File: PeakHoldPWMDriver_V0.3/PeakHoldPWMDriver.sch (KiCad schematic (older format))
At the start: 113 parts, among them J1 RND 205-00203, J2 RND 205-00205, Q1 2N7002, Q10 2N7002, Q11 2N7002, Q12 2N7002, Q13 TSM2309, Q14 IRLL 024N, Q15 TSM2309, Q16 IRLL 024N, Q2 2N7002, Q3 2N7002, Q4 2N7002, Q5 TSM2309, Q6 TSM2309, Q7 IRLL 024N, Q8 IRLL 024N, Q9 2N7002, U1 74LS32, U2 LM2901, U3 74LS74, U4 LTC6992, U5 74LS74, U6 LM340, U7 74LS08, U8 74LS08

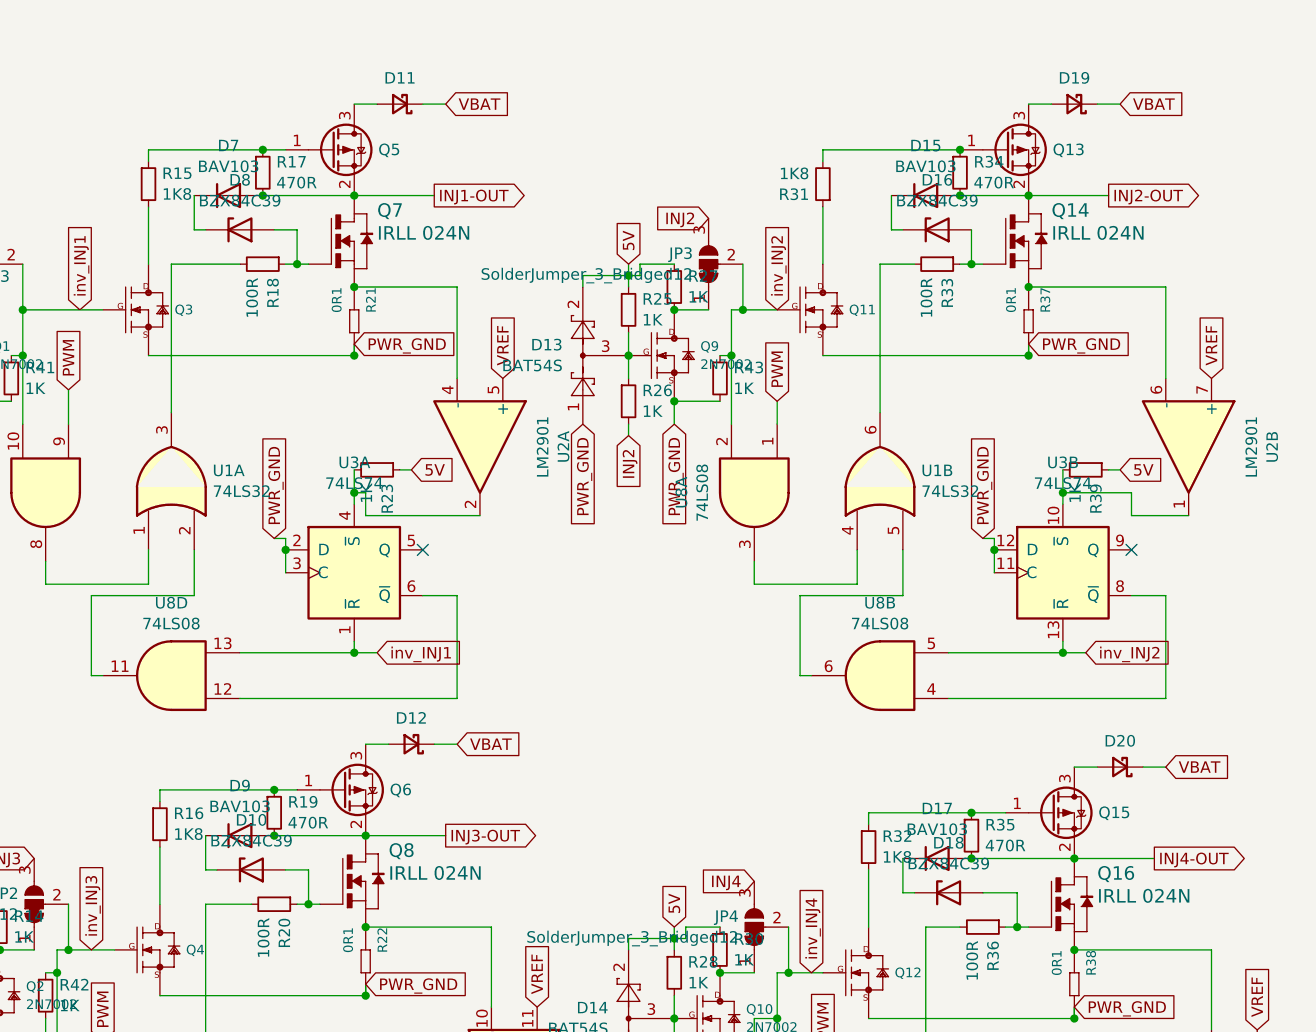
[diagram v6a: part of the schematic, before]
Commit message: update on p-chan mosfets
Overheating issues hopefully solved by this mod
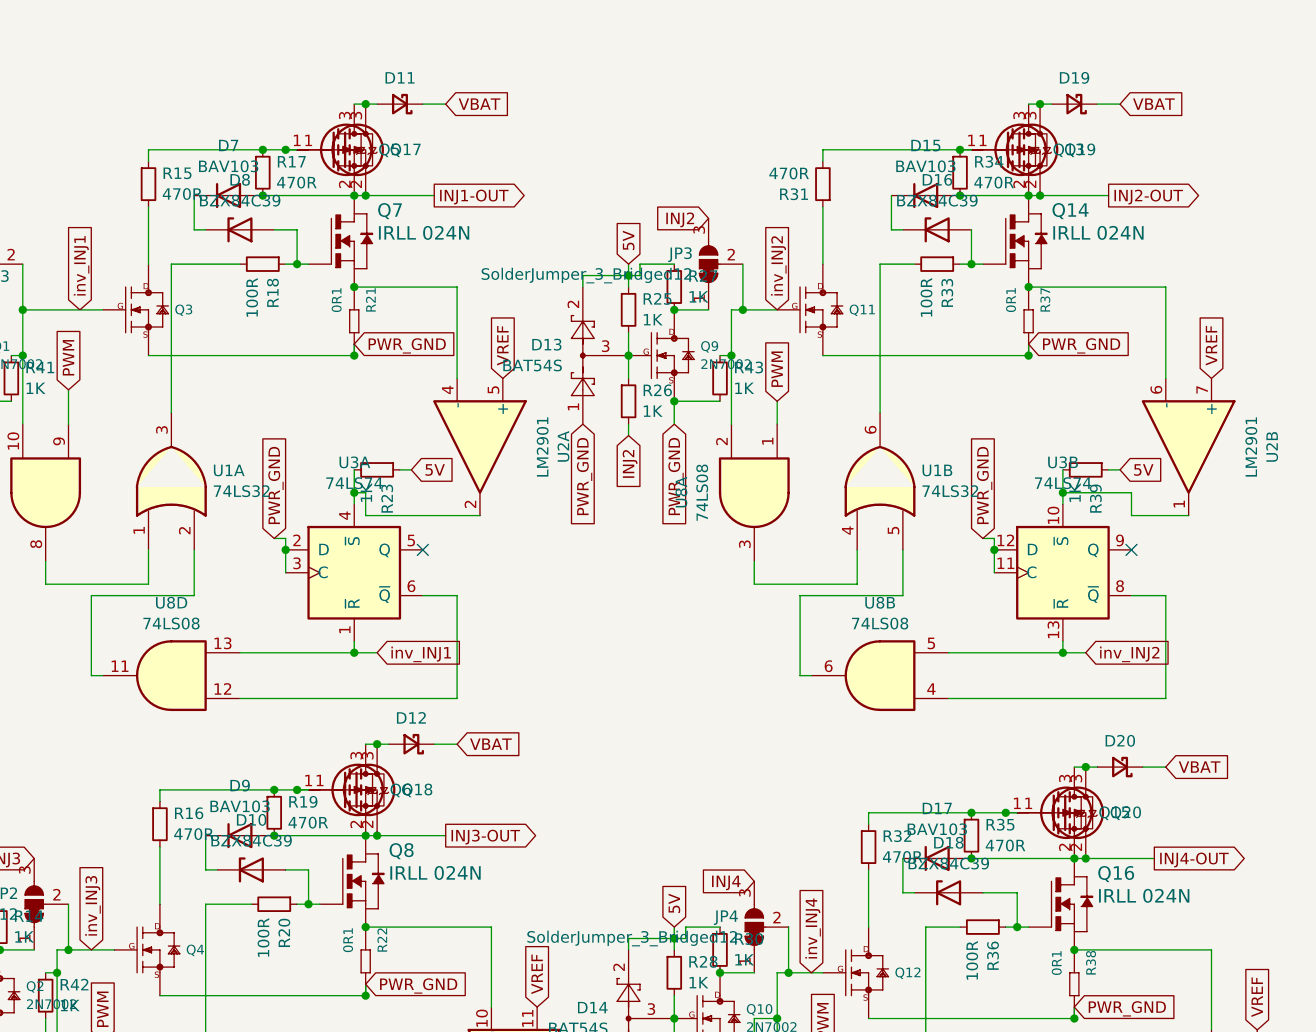
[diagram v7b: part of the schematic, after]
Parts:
- added Q17, Q18, Q19, Q20: TSM2309, Package_TO_SOT_SMD:SOT-23, symbol Transistor_FET:AO3401A
- Q13, Q15, Q5, Q6: footprint Package_TO_SOT_SMD:SOT-23_Handsoldering -> Package_TO_SOT_SMD:SOT-23
- R15, R16, R31, R32: value 1K8 -> 470R
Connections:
- net INJ1-OUT: now also Q17.2 (S)
- net INJ2-OUT: now also Q19.2 (S)
- net INJ3-OUT: now also Q18.2 (S)
- net INJ4-OUT: now also Q20.2 (S)
- net at Q13.1 (G), R31.2, R34.1: now also Q19.1 (G)
- net at D19.2 (A), Q13.3 (D): now also Q19.3 (D)
- net at Q15.1 (G), R32.1, R35.1: now also Q20.1 (G)
- net at Q5.1 (G), R15.1, R17.1: now also Q17.1 (G)
- net at D11.2 (A), Q5.3 (D): now also Q17.3 (D)
- net at Q6.1 (G), R16.1, R19.1: now also Q18.1 (G)
- net at D12.2 (A), Q6.3 (D): now also Q18.3 (D)
- net at D20.2 (A), Q15.3 (D): now also Q20.3 (D)
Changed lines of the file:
@@
 F 0 "Q5" H 7205 1100 50  0000 L CNN
 F 1 "TSM2309" H 7205 1055 50  0001 L CNN
-F 2 "Package_TO_SOT_SMD:SOT-23_Handsoldering" H 7200 1025 50  0001 L CIN
+F 2 "Package_TO_SOT_SMD:SOT-23" H 7200 1025 50  0001 L CIN
 F 3 "https://www.mouser.com/datasheet/2/395/TSM2309_A15-1116136.pdf" H 7000 1100 50  0001 L CNN
 	1    7000 1100
@@
 F 0 "Q15" H 10355 4000 50  0000 L CNN
 F 1 "TSM2309" H 10355 3955 50  0001 L CNN
-F 2 "Package_TO_SOT_SMD:SOT-23_Handsoldering" H 10350 3925 50  0001 L CIN
+F 2 "Package_TO_SOT_SMD:SOT-23" H 10350 3925 50  0001 L CIN
 F 3 "http://www.aosmd.com/pdfs/datasheet/AO3401A.pdf" H 10150 4000 50  0001 L CNN
 	1    10150 4000
@@
 P 9350 4150
 F 0 "R32" H 9409 4196 50  0000 L CNN
-F 1 "1K8" H 9409 4105 50  0000 L CNN
+F 1 "470R" H 9409 4105 50  0000 L CNN
 F 2 "Resistor_SMD:R_0603_1608Metric_Pad1.05x0.95mm_HandSolder" H 9350 4150 50  0001 C CNN
 F 3 "~" H 9350 4150 50  0001 C CNN
@@
 F 0 "Q13" H 10155 1100 50  0000 L CNN
 F 1 "TSM2309" H 10155 1055 50  0001 L CNN
-F 2 "Package_TO_SOT_SMD:SOT-23_Handsoldering" H 10150 1025 50  0001 L CIN
+F 2 "Package_TO_SOT_SMD:SOT-23" H 10150 1025 50  0001 L CIN
 F 3 "http://www.aosmd.com/pdfs/datasheet/AO3401A.pdf" H 9950 1100 50  0001 L CNN
 	1    9950 1100
@@
 F 0 "Q6" H 7255 3900 50  0000 L CNN
 F 1 "TSM2309" H 7255 3855 50  0001 L CNN
-F 2 "Package_TO_SOT_SMD:SOT-23_Handsoldering" H 7250 3825 50  0001 L CIN
+F 2 "Package_TO_SOT_SMD:SOT-23" H 7250 3825 50  0001 L CIN
 F 3 "http://www.aosmd.com/pdfs/datasheet/AO3401A.pdf" H 7050 3900 50  0001 L CNN
 	1    7050 3900
@@
 P 6250 4050
 F 0 "R16" H 6309 4096 50  0000 L CNN
-F 1 "1K8" H 6309 4005 50  0000 L CNN
+F 1 "470R" H 6309 4005 50  0000 L CNN
 F 2 "Resistor_SMD:R_0603_1608Metric_Pad1.05x0.95mm_HandSolder" H 6250 4050 50  0001 C CNN
 F 3 "~" H 6250 4050 50  0001 C CNN
@@
 P 6200 1250
 F 0 "R15" H 6259 1296 50  0000 L CNN
-F 1 "1K8" H 6259 1205 50  0000 L CNN
+F 1 "470R" H 6259 1205 50  0000 L CNN
 F 2 "Resistor_SMD:R_0603_1608Metric_Pad1.05x0.95mm_HandSolder" H 6200 1250 50  0001 C CNN
 F 3 "~" H 6200 1250 50  0001 C CNN
@@
 Connection ~ 7150 4100
 Wire Wire Line
-	7150 3700 7250 3700
+	7150 3700 7200 3700
 Wire Wire Line
 	6250 4400 6250 4150
@@
 PWR_GND
 Wire Wire Line
-	10050 1300 10400 1300
+	10050 1300 10100 1300
 Wire Wire Line
 	10450 900  10350 900
 Connection ~ 10050 1300
 Wire Wire Line
-	10050 900  10150 900
+	10050 900  10100 900
 Wire Wire Line
 	9150 1600 9150 1350
@@
 Connection ~ 10250 4200
 Wire Wire Line
-	10250 3800 10350 3800
+	10250 3800 10300 3800
 Wire Wire Line
 	9350 4500 9350 4250
@@
 Connection ~ 7100 1300
 Wire Wire Line
-	7100 1300 7450 1300
-Wire Wire Line
-	7100 900  7200 900
+	7100 1300 7150 1300
+Wire Wire Line
+	7100 900  7150 900
 Wire Wire Line
 	6700 1300 7100 1300
@@
 	10250 4200 9800 4200
 Wire Wire Line
-	7150 4100 7500 4100
+	7150 4100 7200 4100
 $Comp
 L Comparator:LM2901 U2
@@
 Connection ~ 6750 3900
 Wire Wire Line
-	6750 3900 6850 3900
-Wire Wire Line
 	9350 4000 9800 4000
 Connection ~ 9800 4000
 Wire Wire Line
-	9800 4000 9950 4000
-Wire Wire Line
-	10250 4200 10600 4200
+	10250 4200 10300 4200
 Text GLabel 1500 4350 2    50   Input ~ 0
 5V
@@
 P 9150 1250
 F 0 "R31" H 9209 1296 50  0000 L CNN
-F 1 "1K8" H 9209 1205 50  0000 L CNN
+F 1 "470R" H 9209 1205 50  0000 L CNN
 F 2 "Resistor_SMD:R_0603_1608Metric_Pad1.05x0.95mm_HandSolder" H 9150 1250 50  0001 C CNN
 F 3 "~" H 9150 1250 50  0001 C CNN
@@
 Wire Wire Line
 	5650 2000 5650 2300
+$Comp
+L Transistor_FET:AO3401A Q19
+U 1 1 5F2DA0F5
+P 10000 1100
+F 0 "Q19" H 10205 1100 50  0000 L CNN
+F 1 "TSM2309" H 10205 1055 50  0001 L CNN
+F 2 "Package_TO_SOT_SMD:SOT-23" H 10200 1025 50  0001 L CIN
+F 3 "http://www.aosmd.com/pdfs/datasheet/AO3401A.pdf" H 10000 1100 50  0001 L CNN
+	1    10000 1100
+	1    0    0    -1
+$EndComp
+Connection ~ 10100 1300
+Wire Wire Line
+	10100 1300 10400 1300
+Connection ~ 10100 900
+Wire Wire Line
+	10100 900  10150 900
+Wire Wire Line
+	9800 1100 9750 1100
+$Comp
+L Transistor_FET:AO3401A Q17
+U 1 1 5F30036E
+P 7050 1100
+F 0 "Q17" H 7255 1100 50  0000 L CNN
+F 1 "TSM2309" H 7255 1055 50  0001 L CNN
+F 2 "Package_TO_SOT_SMD:SOT-23" H 7250 1025 50  0001 L CIN
+F 3 "https://www.mouser.com/datasheet/2/395/TSM2309_A15-1116136.pdf" H 7050 1100 50  0001 L CNN
+	1    7050 1100
+	1    0    0    -1
+$EndComp
+Connection ~ 7150 1300
+Wire Wire Line
+	7150 1300 7450 1300
+Connection ~ 7150 900
+Wire Wire Line
+	7150 900  7200 900
+Wire Wire Line
+	6850 1100 6800 1100
+Connection ~ 6800 1100
+$Comp
+L Transistor_FET:AO3401A Q18
+U 1 1 5F324E6B
+P 7100 3900
+F 0 "Q18" H 7305 3900 50  0000 L CNN
+F 1 "TSM2309" H 7305 3855 50  0001 L CNN
+F 2 "Package_TO_SOT_SMD:SOT-23" H 7300 3825 50  0001 L CIN
+F 3 "http://www.aosmd.com/pdfs/datasheet/AO3401A.pdf" H 7100 3900 50  0001 L CNN
+	1    7100 3900
+	1    0    0    -1
+$EndComp
+Connection ~ 7200 4100
+Wire Wire Line
+	7200 4100 7500 4100
+Connection ~ 7200 3700
+Wire Wire Line
+	7200 3700 7250 3700
+Wire Wire Line
+	6750 3900 6850 3900
+Connection ~ 6850 3900
+Wire Wire Line
+	6850 3900 6900 3900
+$Comp
+L Transistor_FET:AO3401A Q20
+U 1 1 5F351A83
+P 10200 4000
+F 0 "Q20" H 10405 4000 50  0000 L CNN
+F 1 "TSM2309" H 10405 3955 50  0001 L CNN
+F 2 "Package_TO_SOT_SMD:SOT-23" H 10400 3925 50  0001 L CIN
+F 3 "http://www.aosmd.com/pdfs/datasheet/AO3401A.pdf" H 10200 4000 50  0001 L CNN
+	1    10200 4000
+	1    0    0    -1
+$EndComp
+Connection ~ 10300 4200
+Wire Wire Line
+	10300 4200 10600 4200
+Connection ~ 10300 3800
+Wire Wire Line
+	10300 3800 10350 3800
+Wire Wire Line
+	9800 4000 9950 4000
+Connection ~ 9950 4000
+Wire Wire Line
+	9950 4000 10000 4000
 $EndSCHEMATC
